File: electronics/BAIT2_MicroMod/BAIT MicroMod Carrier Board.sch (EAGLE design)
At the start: 147 parts, among them J1 SJ-43516-SMT, J10 QWIIC_RIGHT_ANGLE, J15 SM06B-SRSS-TB(LF)(SN), J2 ST-TF-003A, J4 JST_6_PIN_VERTICAL, J5 QWIIC_RIGHT_ANGLE, J6 JST 2PH, J7 MICROMOD-2222-C, SW1 SKQGADE010, SW2 SKQGADE010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

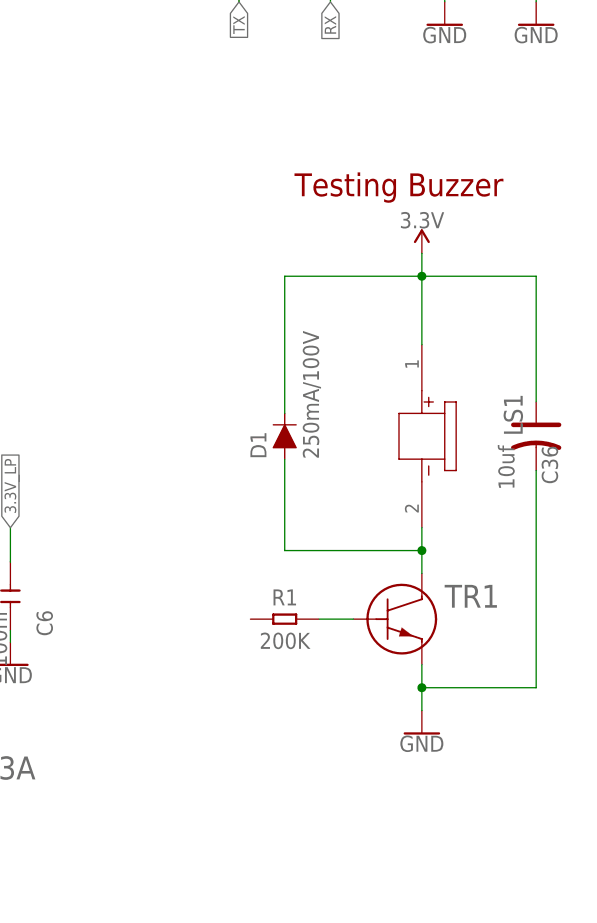
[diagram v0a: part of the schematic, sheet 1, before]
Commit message: Removes testing buzzer
Resolves #21 and partially #14
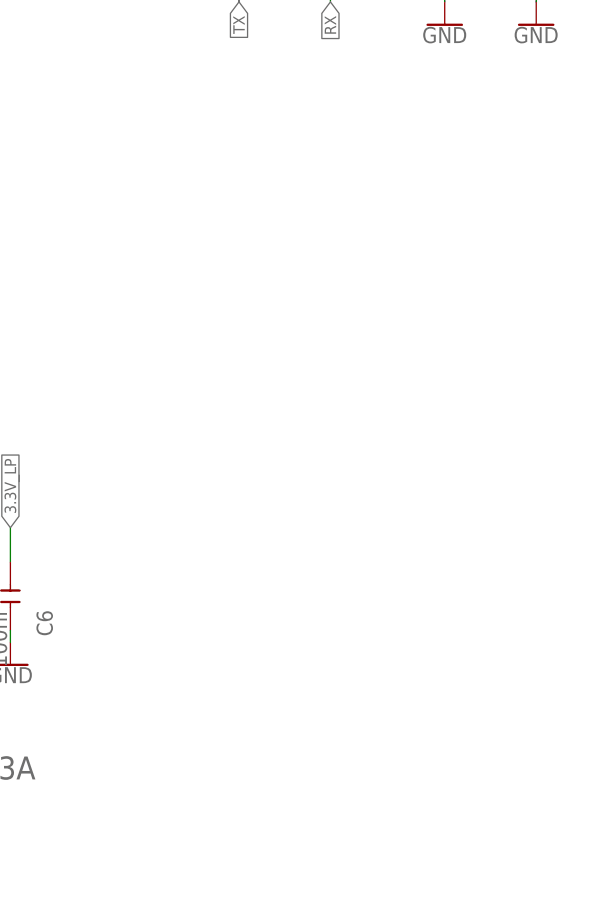
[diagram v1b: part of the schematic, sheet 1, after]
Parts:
- removed C36: 10uf, OPL_Capacitor:TANTALUM-SMD-10UF-16V-10%(AVX-A)
- removed D1: 250mA/100V, SparkFun-DiscreteSemi:DIODE-BAS16J
- removed LS1: CMT-7525-80-SMT-TRCMT-7525-80-SMT-TR_CUD, 2022-07-25_09-48-13_Library:CMT-7525-80-SMT-TRCMT-7525-80-SMT-TR_CUD
- removed R1: 200K, OPL_Resistor:SMD-RES-200K-5%-1/10W(0603)
- removed TR1: MMBT2222A-TPMTR_MMBT2222A-TP_MCE, 2022-07-25_10-23-18_Library:MMBT2222A-TPMTR_MMBT2222A-TP_MCE
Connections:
- removed net N$1: R1.2, TR1.1
- removed net N$2: D1.A, LS1.2, TR1.3
- net 3.3V: no longer C36.+, D1.C, LS1.1
- net GND: no longer C36.-, TR1.2
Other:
- note removed: "Testing Buzzer"
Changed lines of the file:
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@@
 <schematic_group name="WIRELESS"/>
 <schematic_group name="PORTS"/>
-<schematic_group name="TESTING"/>
 <schematic_group name="CODEC"/>
 </groups>
@@
 <part name="GND9" library="SparkFun-PowerSymbols" deviceset="GND" device=""/>
 <part name="GND12" library="SparkFun-PowerSymbols" deviceset="GND" device=""/>
-<part name="LS1" library="2022-07-25_09-48-13_Library" deviceset="CMT-7525-80-SMT-TR" device="CMT-7525-80-SMT-TR_CUD">
-<attribute name="MPN" value="102-CMT-7525-80-SMT-TR-ND"/>
-</part>
-<part name="GND2" library="SparkFun-PowerSymbols" library_urn="urn:adsk.eagle:library:530" deviceset="GND" device=""/>
-<part name="SUPPLY10" library="SparkFun-PowerSymbols" library_urn="urn:adsk.eagle:library:530" deviceset="3.3V" device=""/>
-<part name="TR1" library="2022-07-25_10-23-18_Library" deviceset="MMBT2222A-TP" device="MTR_MMBT2222A-TP_MCE">
-<attribute name="MPN" value="MMBT2222ATPMSTR-ND"/>
-</part>
-<part name="R1" library="OPL_Resistor" library_urn="urn:adsk.eagle:library:8004883" deviceset="SMD-RES-200K-5%-1/10W(0603)" device="" package3d_urn="urn:adsk.eagle:package:8004941/1" value="200K"/>
-<part name="D1" library="SparkFun-DiscreteSemi" library_urn="urn:adsk.eagle:library:514" deviceset="DIODE" device="-BAS16J" package3d_urn="urn:adsk.eagle:package:38441/1" value="250mA/100V">
-<attribute name="MPN" value="BAS16J,115"/>
-</part>
 <part name="G1" library="Power or GND " deviceset="GND_POWER" device=""/>
 <part name="J_ASC" library="SparkFun-Jumpers" deviceset="JUMPER-SMT_2_NC_TRACE" device="_SILK" package3d_urn="urn:adsk.eagle:package:39281/1" value=""/>
@@
 </part>
 <part name="G2" library="Power or GND " deviceset="GND_POWER" device=""/>
-<part name="C36" library="OPL_Capacitor" library_urn="urn:adsk.eagle:library:8004261" deviceset="TANTALUM-SMD-10UF-16V-10%(AVX-A)" device="" package3d_urn="urn:adsk.eagle:package:8004284/1" value="10uf"/>
 <part name="U$3" library="SparkFun-PowerSymbols" library_urn="urn:adsk.eagle:library:530" deviceset="AGND" device=""/>
 <part name="U$4" library="SparkFun-PowerSymbols" library_urn="urn:adsk.eagle:library:530" deviceset="AGND" device=""/>
@@
 <text x="274.32" y="88.9" size="2.54" layer="94" align="center" grouprefs="USD">μSD</text>
 <text x="165.354" y="246.126" size="2.54" layer="94" font="vector" align="center" grouprefs="PORTS">I2S Port</text>
-<text x="358.14" y="104.14" size="2.54" layer="94" align="center" grouprefs="TESTING">Testing Buzzer</text>
 <text x="292.354" y="157.226" size="2.54" layer="94" font="vector" align="center" grouprefs="WIRELESS">XBee</text>
 <text x="259.334" y="180.086" size="2.54" layer="94" font="vector" align="center" grouprefs="WIRELESS">SWO</text>
@@
 <attribute name="MPN" x="167.64" y="231.14" size="1.27" layer="96" display="off"/>
 </instance>
-<instance part="LS1" gate="A" x="360.68" y="88.9" smashed="yes" rot="R270" grouprefs="TESTING">
-<attribute name="NAME" x="369.7986" y="80.9254" size="2.083" layer="95" ratio="6" rot="R270"/>
-<attribute name="MPN" x="360.68" y="88.9" size="1.27" layer="96" rot="R270" display="off"/>
-</instance>
-<instance part="GND2" gate="1" x="360.68" y="43.18" smashed="yes" grouprefs="TESTING">
-<attribute name="VALUE" x="360.68" y="42.926" size="1.778" layer="96" align="top-center"/>
-</instance>
-<instance part="SUPPLY10" gate="G$1" x="360.68" y="96.52" smashed="yes" grouprefs="TESTING">
-<attribute name="VALUE" x="360.68" y="99.314" size="1.778" layer="96" align="bottom-center"/>
-</instance>
-<instance part="TR1" gate="A" x="353.06" y="55.88" smashed="yes" grouprefs="TESTING">
-<attribute name="NAME" x="363.22" y="57.15" size="2.54" layer="95" ratio="10"/>
-<attribute name="MPN" x="353.06" y="55.88" size="1.27" layer="96" display="off"/>
-</instance>
-<instance part="R1" gate="G$1" x="345.44" y="55.88" smashed="yes" grouprefs="TESTING">
-<attribute name="NAME" x="345.44" y="57.404" size="1.778" layer="95" font="vector" align="bottom-center"/>
-<attribute name="VALUE" x="345.44" y="54.356" size="1.778" layer="96" font="vector" align="top-center"/>
-</instance>
-<instance part="D1" gate="G$1" x="345.44" y="76.2" smashed="yes" rot="R90" grouprefs="TESTING">
-<attribute name="NAME" x="343.408" y="73.66" size="1.778" layer="95" font="vector" rot="R90"/>
-<attribute name="VALUE" x="347.472" y="73.66" size="1.778" layer="96" font="vector" rot="R90" align="top-left"/>
-<attribute name="MPN" x="345.44" y="76.2" size="1.27" layer="96" rot="R90" display="off"/>
-</instance>
 <instance part="G1" gate="G$1" x="264.16" y="121.92" smashed="yes" grouprefs="WIRELESS"/>
 <instance part="J_ASC" gate="G$1" x="373.38" y="154.94" smashed="yes" rot="R90" grouprefs="WIRELESS">
@@
 </instance>
 <instance part="G2" gate="G$1" x="248.92" y="129.54" smashed="yes" grouprefs="WIRELESS"/>
-<instance part="C36" gate="G$1" x="373.38" y="76.2" smashed="yes" rot="R270" grouprefs="TESTING">
-<attribute name="NAME" x="374.015" y="75.184" size="1.778" layer="95" font="vector" rot="R270"/>
-<attribute name="VALUE" x="369.189" y="75.184" size="1.778" layer="96" font="vector" rot="R270"/>
-</instance>
 <instance part="SW1" gate="G$1" x="101.6" y="231.14" smashed="yes" grouprefs="MICROMOD">
 <attribute name="NAME" x="96.52" y="236.22" size="1.27" layer="95" ratio="10"/>
@@
 </segment>
 <segment>
-<pinref part="TR1" gate="A" pin="2"/>
-<pinref part="GND2" gate="1" pin="GND"/>
-<wire x1="360.68" y1="50.8" x2="360.68" y2="48.26" width="0.1524" layer="91" grouprefs="TESTING"/>
-<wire x1="360.68" y1="48.26" x2="360.68" y2="45.72" width="0.1524" layer="91" grouprefs="TESTING"/>
-<wire x1="373.38" y1="72.39" x2="373.38" y2="48.26" width="0.1524" layer="91" grouprefs="TESTING"/>
-<wire x1="373.38" y1="48.26" x2="360.68" y2="48.26" width="0.1524" layer="91" grouprefs="TESTING"/>
-<pinref part="C36" gate="G$1" pin="-"/>
-<junction x="360.68" y="48.26"/>
-</segment>
-<segment>
 <pinref part="G1" gate="G$1" pin="GND"/>
 <wire x1="264.16" y1="124.46" x2="264.16" y2="121.92" width="0.1524" layer="91" grouprefs="WIRELESS"/>
@@
 <wire x1="262.89" y1="222.25" x2="256.54" y2="222.25" width="0.1524" layer="91" grouprefs="WIRELESS"/>
 <label x="256.54" y="222.25" size="0.889" layer="95" ratio="12" rot="R180" xref="yes" grouprefs="WIRELESS"/>
-</segment>
-<segment>
-<pinref part="SUPPLY10" gate="G$1" pin="3.3V"/>
-<pinref part="LS1" gate="A" pin="1"/>
-<wire x1="360.68" y1="86.36" x2="360.68" y2="93.98" width="0.1524" layer="91" grouprefs="TESTING"/>
-<pinref part="D1" gate="G$1" pin="C"/>
-<wire x1="360.68" y1="93.98" x2="360.68" y2="96.52" width="0.1524" layer="91" grouprefs="TESTING"/>
-<wire x1="345.44" y1="78.74" x2="345.44" y2="93.98" width="0.1524" layer="91" grouprefs="TESTING"/>
-<wire x1="345.44" y1="93.98" x2="360.68" y2="93.98" width="0.1524" layer="91"/>
-<wire x1="373.38" y1="80.01" x2="373.38" y2="93.98" width="0.1524" layer="91" grouprefs="TESTING"/>
-<pinref part="C36" gate="G$1" pin="+"/>
-<wire x1="373.38" y1="93.98" x2="360.68" y2="93.98" width="0.1524" layer="91"/>
-<junction x="360.68" y="93.98"/>
 </segment>
 <segment>
@@
 </segment>
 </net>
-<net name="N$1" class="0">
-<segment>
-<pinref part="R1" gate="G$1" pin="2"/>
-<pinref part="TR1" gate="A" pin="1"/>
-<wire x1="349.25" y1="55.88" x2="353.06" y2="55.88" width="0.1524" layer="91" grouprefs="TESTING"/>
-</segment>
-</net>
-<net name="N$2" class="0">
-<segment>
-<pinref part="TR1" gate="A" pin="3"/>
-<pinref part="LS1" gate="A" pin="2"/>
-<wire x1="360.68" y1="60.96" x2="360.68" y2="63.5" width="0.1524" layer="91" grouprefs="TESTING"/>
-<pinref part="D1" gate="G$1" pin="A"/>
-<wire x1="345.44" y1="73.66" x2="345.44" y2="63.5" width="0.1524" layer="91" grouprefs="TESTING"/>
-<wire x1="345.44" y1="63.5" x2="360.68" y2="63.5" width="0.1524" layer="91" grouprefs="TESTING"/>
-<wire x1="360.68" y1="63.5" x2="360.68" y2="66.04" width="0.1524" layer="91" grouprefs="TESTING"/>
-<junction x="360.68" y="63.5"/>
-</segment>
-</net>

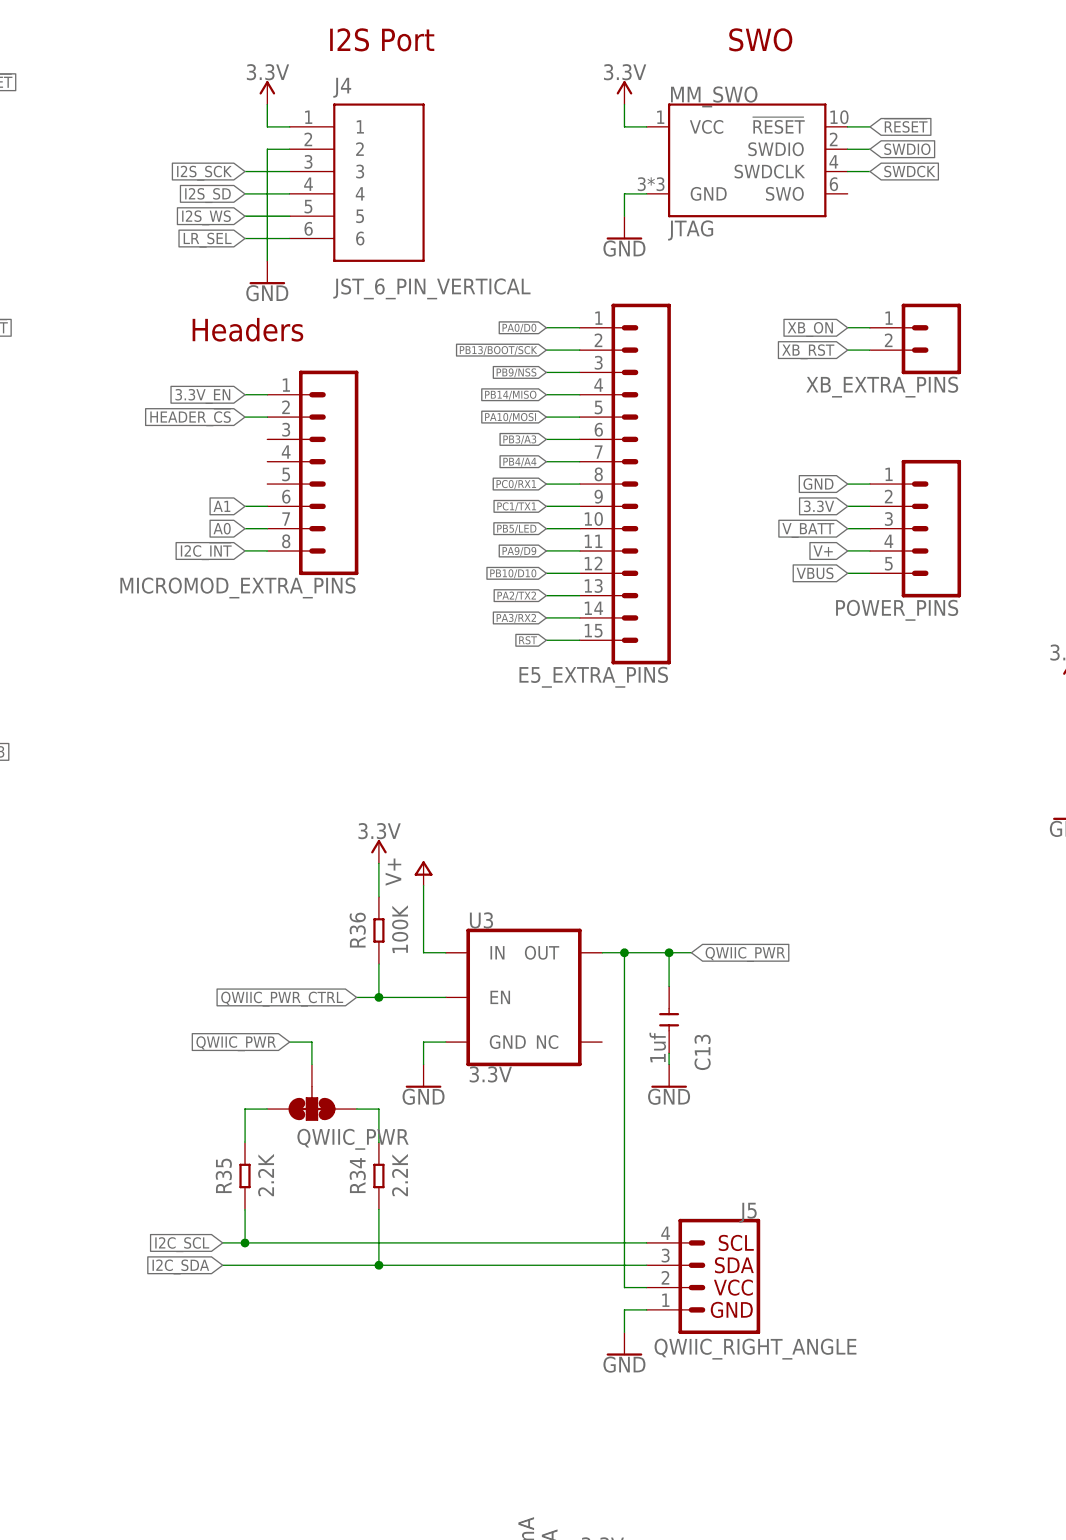
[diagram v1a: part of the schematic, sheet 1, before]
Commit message: Updated the JST connectors
Switched to the correct (vertical orientation) connector and swapped the 6-pin audio connector for a 5-pin version
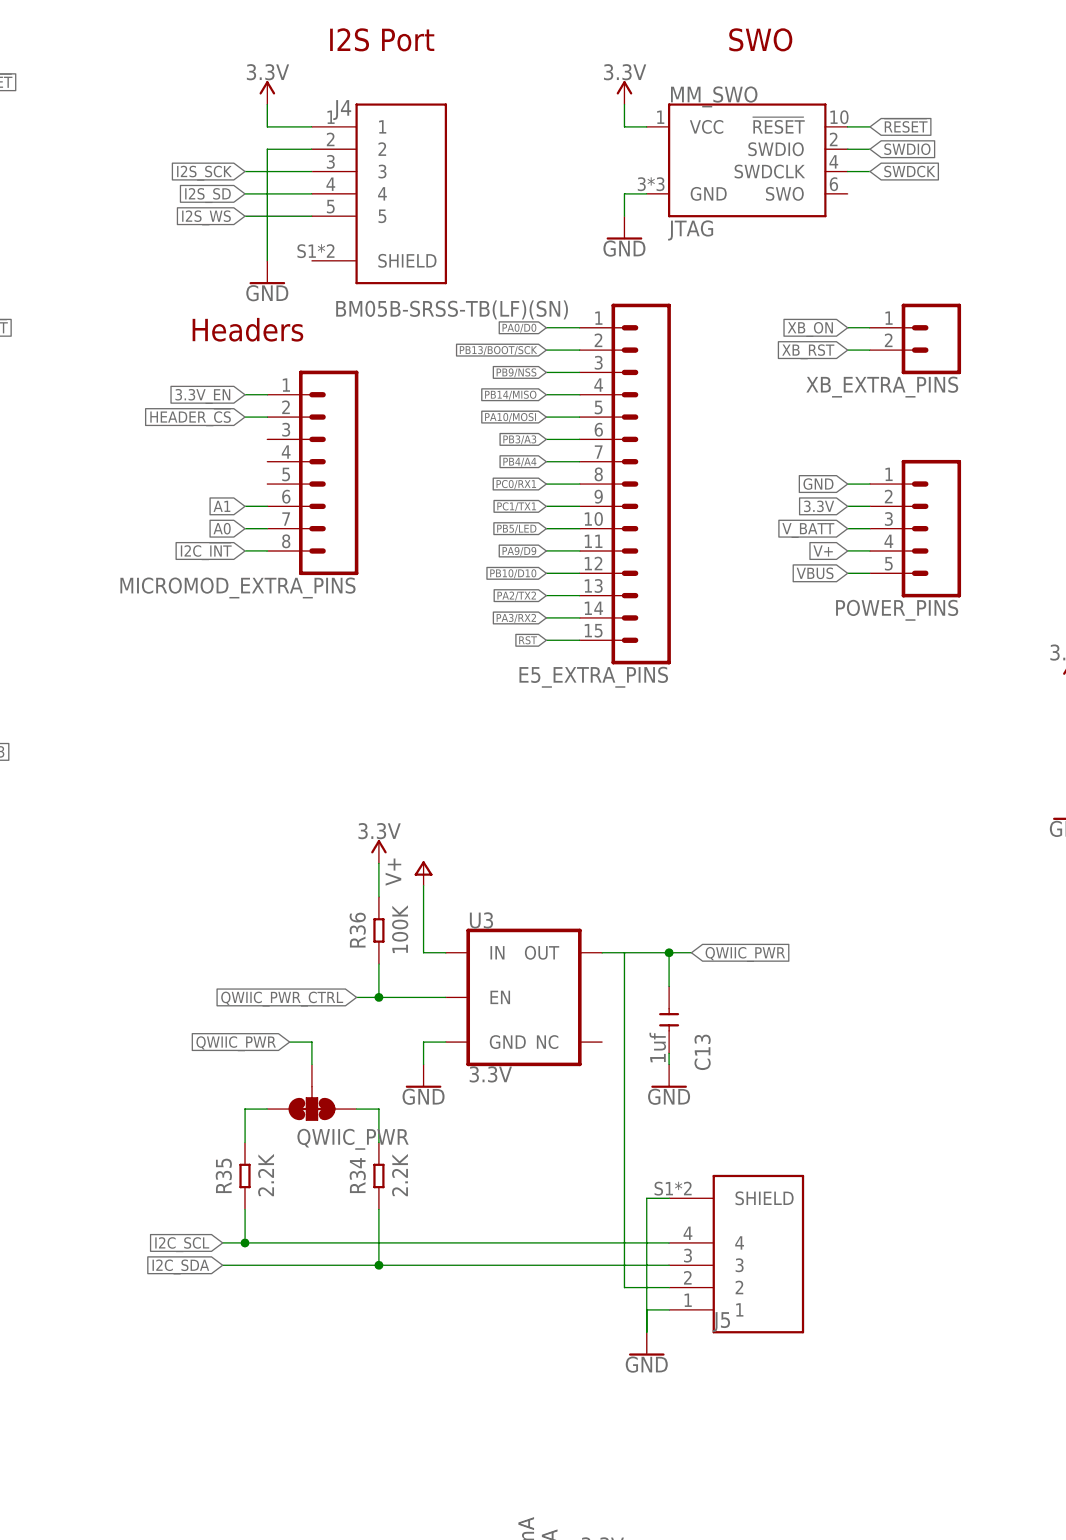
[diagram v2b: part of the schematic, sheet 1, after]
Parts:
- J10: device SM04B-SRSS-TB_LF__SN_:SM04B-SRSS-TB(LF)(SN) -> JST SH Connectors:BM04B-SRSS-TB(LF)(SN)
- J15: value SM06B-SRSS-TB(LF)(SN) -> BM05B-SRSS-TB(LF)(SN); device SM06B-SRSS-TB_LF__SN_:SM06B-SRSS-TB(LF)(SN) -> JST SH Connectors:BM05B-SRSS-TB(LF)(SN)
- J4: value JST_6_PIN_VERTICAL -> BM05B-SRSS-TB(LF)(SN); device SparkFun-Connectors:JST_6_PIN_VERTICAL -> JST SH Connectors:BM05B-SRSS-TB(LF)(SN)
- J5: device SparkFun-Connectors:QWIIC_CONNECTORJS-1MM -> JST SH Connectors:BM04B-SRSS-TB(LF)(SN)
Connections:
- net GND: now also J5.SHIELD
- net LR_SEL: no longer J4.6
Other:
- moved on the sheet: J4

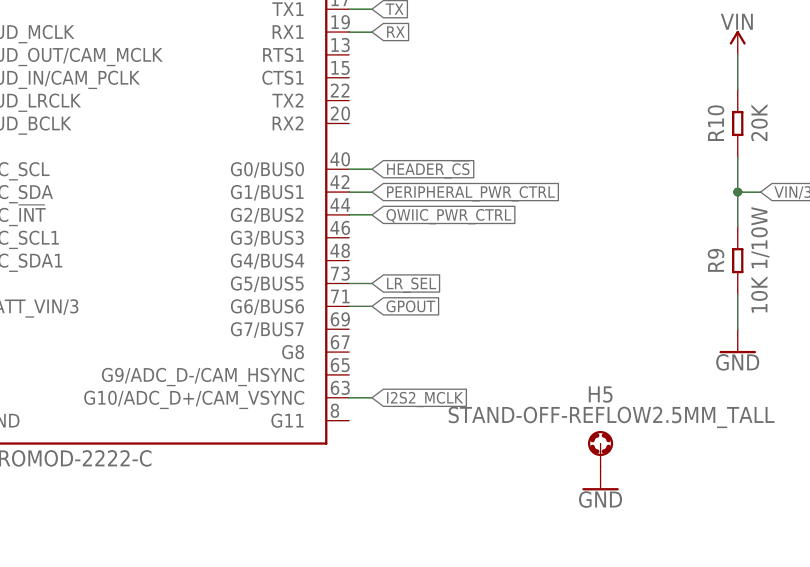
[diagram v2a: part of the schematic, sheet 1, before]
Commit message: Also removed LR_SEL from MicroMod schematic
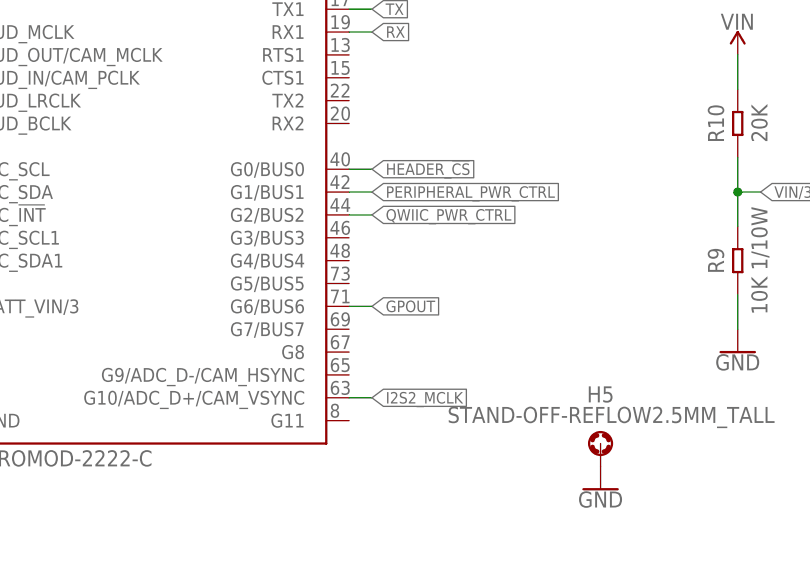
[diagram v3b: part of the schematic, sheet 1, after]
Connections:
- removed net LR_SEL: J7.G5/BUS5
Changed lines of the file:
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@@
-</segment>
-</net>
-<net name="LR_SEL" class="0">
-<segment>
-<pinref part="J7" gate="J1" pin="G5/BUS5"/>
-<wire x1="71.12" y1="154.94" x2="73.66" y2="154.94" width="0.1524" layer="91" grouprefs="MICROMOD"/>
-<label x="73.66" y="154.94" size="1.27" layer="95" xref="yes" grouprefs="MICROMOD"/>
 </segment>
 </net>
